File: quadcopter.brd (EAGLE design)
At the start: 128 x 128 mm, 67 parts, among them J1 ISP, J4 SIP-10_TH-254X10, M1 MOTOR_PADS, M2 MOTOR_PADS, M3 MOTOR_PADS, M4 MOTOR_PADS, SW1 PUSHBUTTON_SMD-VERTICAL-1, U1 ATMEGA128RFA1, Y1 16MHz

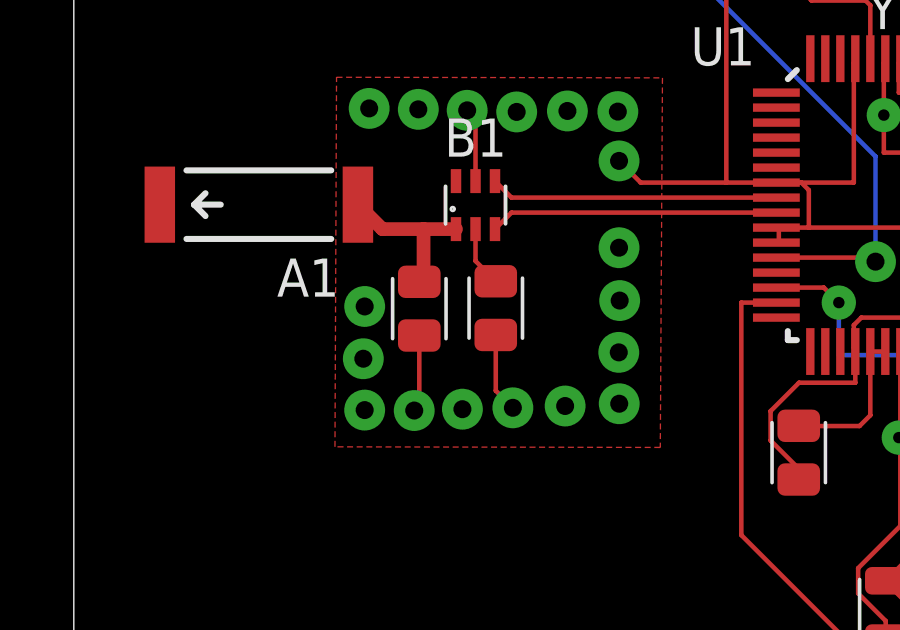
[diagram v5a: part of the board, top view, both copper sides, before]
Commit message: new board after Prof.'s review on May 10th
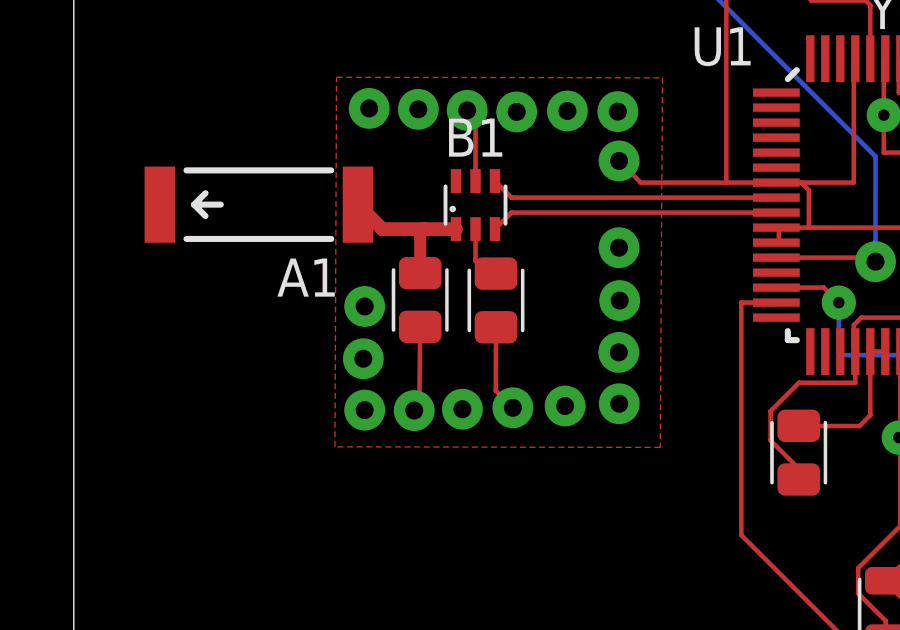
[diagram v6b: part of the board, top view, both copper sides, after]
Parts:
- moved C17 0.29 mm to (-38.5, -3.16)
- moved C15 0.26 mm to (-35.9, -3.18)
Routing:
- net GND: track 456.6 -> 457.2 mm
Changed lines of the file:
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@@
 <attribute name="MPN" value="GRM21A5C2E120JW01D" x="-20.88" y="12.74" size="1.778" layer="27" display="off"/>
 </element>
-<element name="C15" library="quadparts_prebuilt" package="CAPC2012X140_HS" value="22pF" x="-35.935" y="-3.434" rot="R270">
-<attribute name="CREATOR" value="PROF" x="-35.935" y="-3.434" size="1.778" layer="27" rot="R270" display="off"/>
-<attribute name="DIST" value="Digikey" x="-35.935" y="-3.434" size="1.778" layer="27" rot="R270" display="off"/>
-<attribute name="DISTPN" value="490-5534-1-ND" x="-35.935" y="-3.434" size="1.778" layer="27" rot="R270" display="off"/>
-<attribute name="MFR" value="Murata Electronics North America" x="-35.935" y="-3.434" size="1.778" layer="27" rot="R270" display="off"/>
-<attribute name="MPN" value="GRM21A5C2E220JW01D" x="-35.935" y="-3.434" size="1.778" layer="27" rot="R270" display="off"/>
-<attribute name="REVIEWER" value="" x="-35.935" y="-3.434" size="1.778" layer="27" rot="R270" display="off"/>
+<element name="C15" library="quadparts_prebuilt" package="CAPC2012X140_HS" value="22pF" x="-35.928" y="-3.178" rot="R270">
+<attribute name="CREATOR" value="PROF" x="-35.928" y="-3.178" size="1.778" layer="27" rot="R270" display="off"/>
+<attribute name="DIST" value="Digikey" x="-35.928" y="-3.178" size="1.778" layer="27" rot="R270" display="off"/>
+<attribute name="DISTPN" value="490-5534-1-ND" x="-35.928" y="-3.178" size="1.778" layer="27" rot="R270" display="off"/>
+<attribute name="MFR" value="Murata Electronics North America" x="-35.928" y="-3.178" size="1.778" layer="27" rot="R270" display="off"/>
+<attribute name="MPN" value="GRM21A5C2E220JW01D" x="-35.928" y="-3.178" size="1.778" layer="27" rot="R270" display="off"/>
+<attribute name="REVIEWER" value="" x="-35.928" y="-3.178" size="1.778" layer="27" rot="R270" display="off"/>
 </element>
 <element name="C16" library="quadparts_prebuilt" package="CAPC2012X140_HS" value="0.1uF" x="6.74" y="37.61" rot="R270">
@@
 <attribute name="REVIEWER" value="" x="6.74" y="37.61" size="1.778" layer="27" rot="R270" display="off"/>
 </element>
-<element name="C17" library="quadparts_prebuilt" package="CAPC2012X140_HS" value="0.75pF" x="-38.484" y="-3.452" rot="R90">
-<attribute name="DIST" value="Digikey" x="-38.484" y="-3.452" size="1.778" layer="27" rot="R90" display="off"/>
-<attribute name="DISTPN" value="490-3585-1-ND" x="-38.484" y="-3.452" size="1.778" layer="27" rot="R90" display="off"/>
-<attribute name="MFR" value="Murata Electronics North America" x="-38.484" y="-3.452" size="1.778" layer="27" rot="R90" display="off"/>
-<attribute name="MPN" value="GQM2195C2AR75CB01D" x="-38.484" y="-3.452" size="1.778" layer="27" rot="R90" display="off"/>
+<element name="C17" library="quadparts_prebuilt" package="CAPC2012X140_HS" value="0.75pF" x="-38.453" y="-3.163" rot="R90">
+<attribute name="DIST" value="Digikey" x="-38.453" y="-3.163" size="1.778" layer="27" rot="R90" display="off"/>
+<attribute name="DISTPN" value="490-3585-1-ND" x="-38.453" y="-3.163" size="1.778" layer="27" rot="R90" display="off"/>
+<attribute name="MFR" value="Murata Electronics North America" x="-38.453" y="-3.163" size="1.778" layer="27" rot="R90" display="off"/>
+<attribute name="MPN" value="GQM2195C2AR75CB01D" x="-38.453" y="-3.163" size="1.778" layer="27" rot="R90" display="off"/>
 </element>
 <element name="C18" library="quadparts_prebuilt" package="CAPC2012X140_HS" value="1uF" x="11.82" y="-16.16" rot="R90">
@@
 <via x="-40.35" y="-5.121" extent="1-16" drill="0.6"/>
 <via x="-40.305" y="-3.379" extent="1-16" drill="0.6"/>
-<wire x1="-38.484" y1="-4.347" x2="-38.484" y2="-6.679" width="0.1524" layer="1"/>
+<wire x1="-38.453" y1="-4.058" x2="-38.484" y2="-6.679" width="0.1524" layer="1"/>
 <wire x1="-38.484" y1="-6.679" x2="-38.653" y2="-6.848" width="0.1524" layer="1"/>
-<wire x1="-35.935" y1="-4.329" x2="-35.935" y2="-6.187" width="0.1524" layer="1"/>
+<wire x1="-35.928" y1="-4.073" x2="-35.935" y2="-6.187" width="0.1524" layer="1"/>
 <wire x1="-35.935" y1="-6.187" x2="-35.365" y2="-6.757" width="0.1524" layer="1"/>
 <wire x1="-36.61" y1="0.8" x2="-36.61" y2="2.881" width="0.1524" layer="1"/>
@@
 <contactref element="C17" pad="2"/>
 <contactref element="A1" pad="FEED"/>
-<wire x1="-37.26" y1="-0.8" x2="-38.343" y2="-0.8" width="0.4572" layer="1"/>
-<wire x1="-38.343" y1="-0.8" x2="-39.715" y2="-0.8" width="0.4572" layer="1"/>
+<wire x1="-37.26" y1="-0.8" x2="-38.319" y2="-0.8" width="0.4572" layer="1"/>
+<wire x1="-38.319" y1="-0.8" x2="-39.715" y2="-0.8" width="0.4572" layer="1"/>
 <wire x1="-39.715" y1="-0.8" x2="-40.53" y2="0.015" width="0.4572" layer="1"/>
-<wire x1="-38.343" y1="-0.8" x2="-38.343" y2="-2.416" width="0.4572" layer="1"/>
-<wire x1="-38.343" y1="-2.416" x2="-38.484" y2="-2.557" width="0.4572" layer="1"/>
+<wire x1="-38.453" y1="-2.268" x2="-38.343" y2="-2.416" width="0.4572" layer="1"/>
+<wire x1="-38.319" y1="-0.8" x2="-38.453" y2="-0.8" width="0.4064" layer="1"/>
+<wire x1="-38.453" y1="-0.8" x2="-38.453" y2="-2.268" width="0.4064" layer="1"/>
 </signal>
 <signal name="RESET">
@@
 <contactref element="C15" pad="1"/>
 <wire x1="-36.61" y1="-0.8" x2="-36.61" y2="-1.864" width="0.1524" layer="1"/>
-<wire x1="-36.61" y1="-1.864" x2="-35.935" y2="-2.539" width="0.1524" layer="1"/>
+<wire x1="-36.61" y1="-1.864" x2="-35.928" y2="-2.283" width="0.1524" layer="1"/>
 </signal>
 <signal name="N$16">

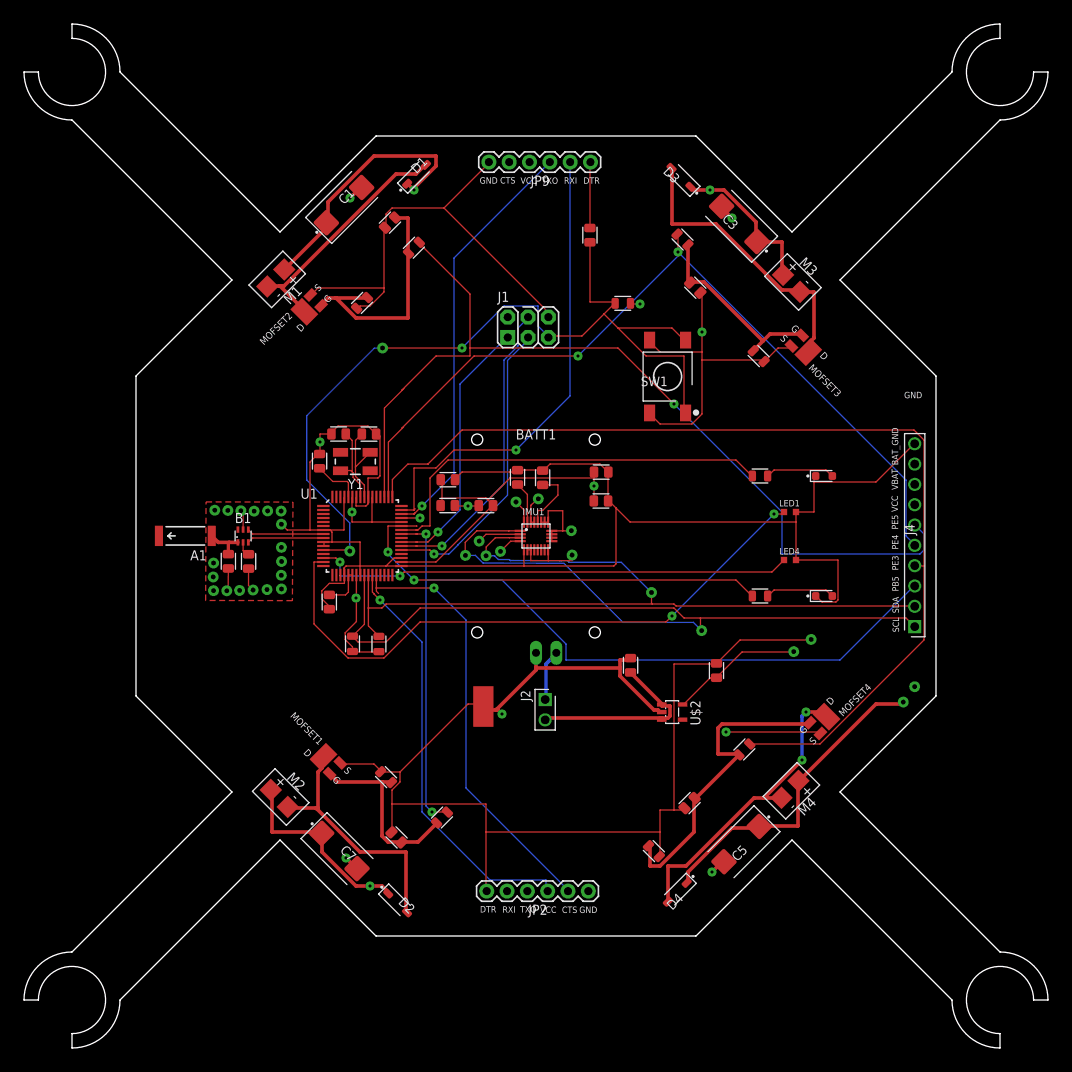
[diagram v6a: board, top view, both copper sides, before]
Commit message: New board with de cap connecting to microcon
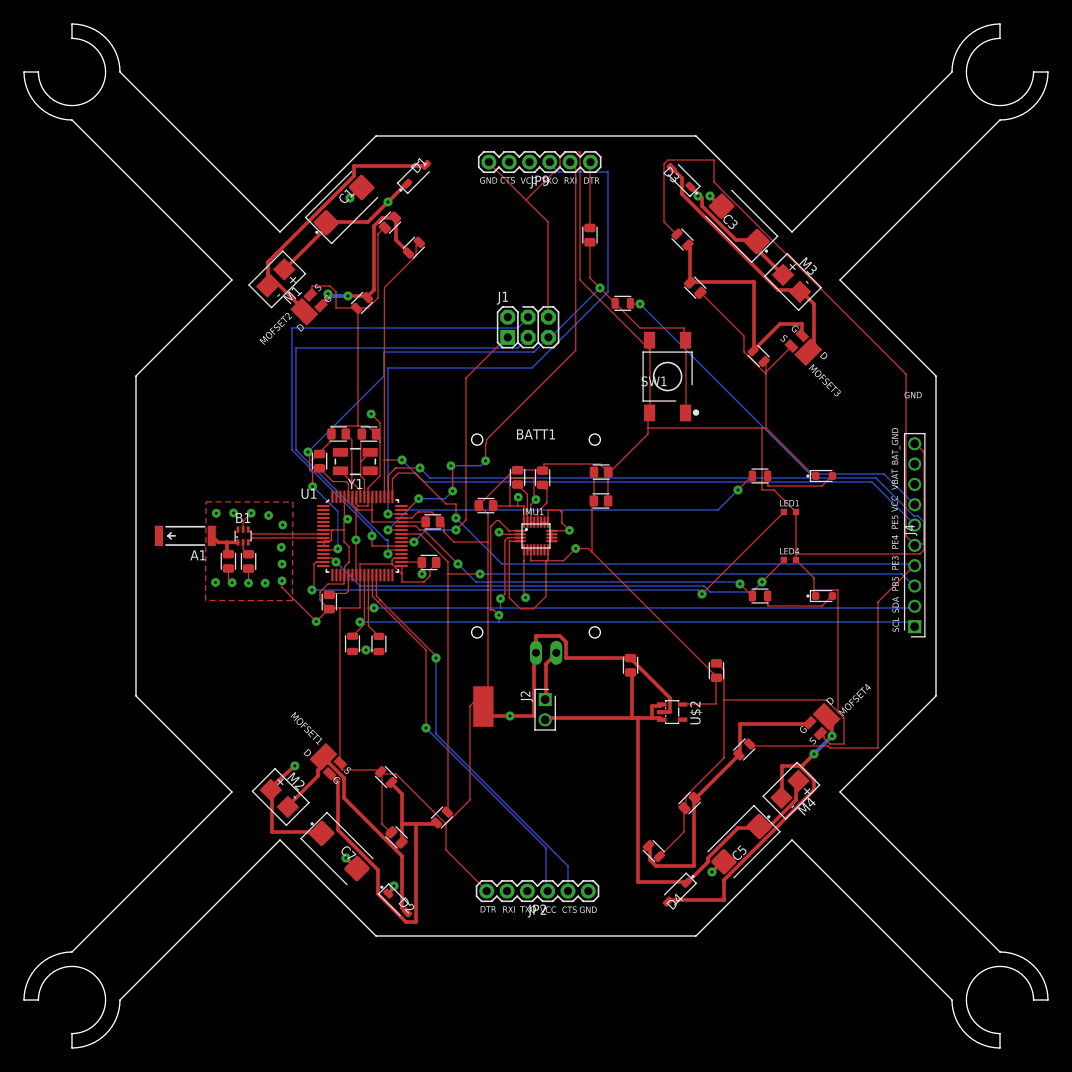
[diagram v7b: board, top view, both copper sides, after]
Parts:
- moved C11 10.6 mm to (-13.4, -3.31)
- moved C12 2.77 mm to (-12.9, 1.76)
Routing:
- net GND: track 457.2 -> 534.0 mm, vias 25 -> 17
- net VCC: track 119.2 -> 168.1 mm, vias 10 -> 8
- net PE4: track 104.5 -> 151.4 mm, vias 2 -> 1
- net SCL: track 125.7 -> 95.5 mm
- net MOSI: track 38.1 -> 65.2 mm
- net FILTERED_1: track 23.1 -> 48.4 mm
- net SCK: track 37.3 -> 62.4 mm
- net RX0: track 52.8 -> 74.3 mm
- net SDA: track 106.8 -> 87.4 mm
- net RESET: track 110.8 -> 91.9 mm, vias 3 -> 4
- net VBAT: track 142.2 -> 125.7 mm
- net PB5: track 110.3 -> 97.6 mm, vias 2 -> 1
- net PE5: track 116.0 -> 103.4 mm
- net PE3: track 125.1 -> 115.0 mm, vias 0 -> 1
- net PG1: track 77.0 -> 68.1 mm
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
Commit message: new board modified decoupling cap for imu
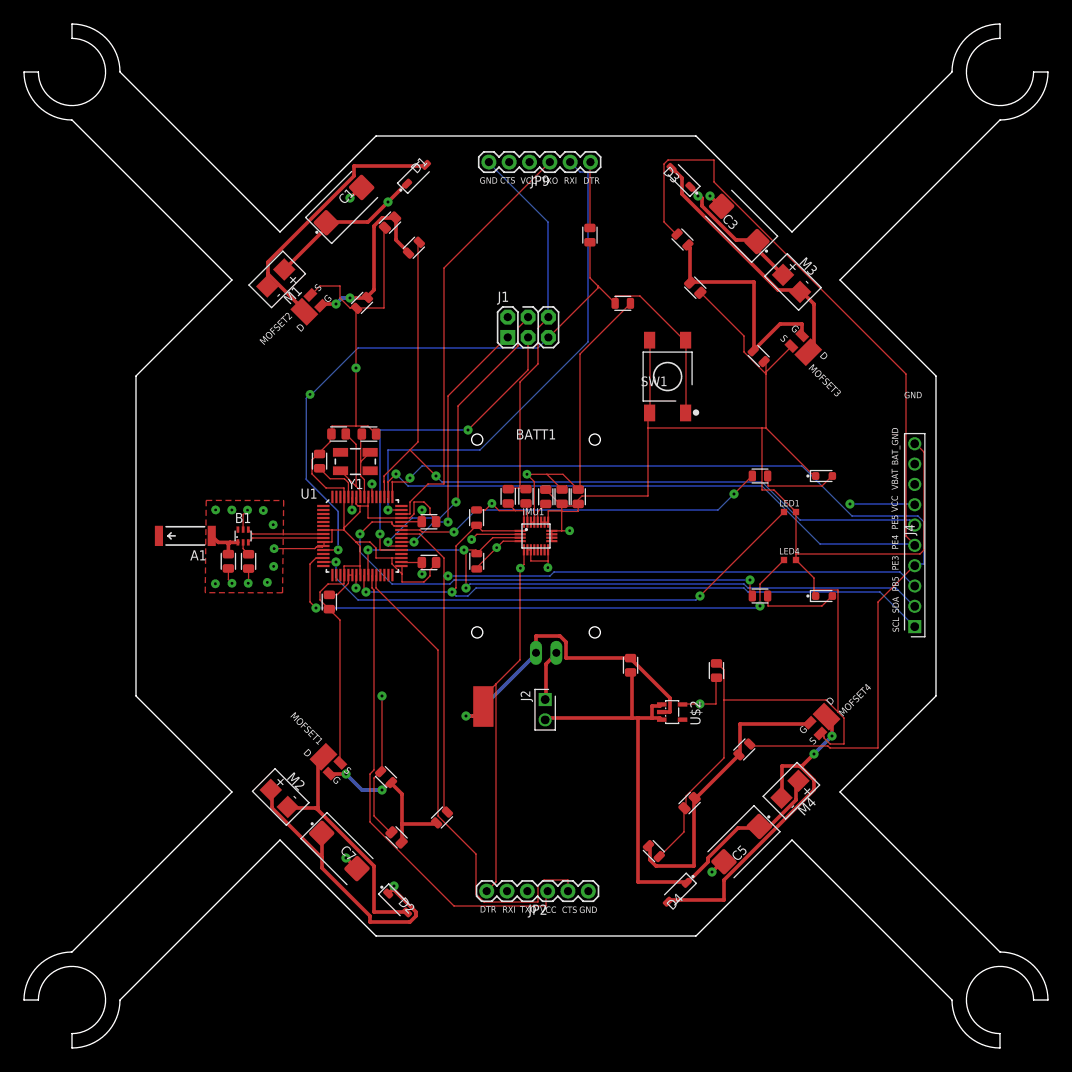
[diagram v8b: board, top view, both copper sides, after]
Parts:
- moved R14 22.1 mm to (-7.42, 2.30), turned to 90 degrees
- moved R15 16.0 mm to (-7.41, -3.16)
- moved C23 4.88 mm to (3.27, 4.92), turned to 90 degrees
- moved C22 4.21 mm to (5.28, 4.91), turned to 90 degrees
- moved C24 3.02 mm to (-3.48, 4.96), turned to 90 degrees
- moved C21 2.59 mm to (-1.26, 4.96)
- moved C20 2.41 mm to (1.22, 4.90)
- moved C12 0.49 mm to (-13.4, 1.78)
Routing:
- net VCC: track 168.1 -> 100.1 mm, vias 8 -> 12
- net GND: track 534.0 -> 488.0 mm, vias 17 -> 15
- net FILTERED_1: track 48.4 -> 21.5 mm, vias 0 -> 2
- net MOSI: track 65.2 -> 39.6 mm, vias 1 -> 2
- net RX0: track 74.3 -> 53.5 mm, vias 1 -> 0
- net VBAT: track 125.7 -> 145.4 mm, vias 4 -> 3
- net SCK: track 62.4 -> 43.4 mm, vias 1 -> 2
- net PB7: track 47.5 -> 61.2 mm
- net N$4: track 49.7 -> 60.7 mm, vias 1 -> 0
- net N$5: track 48.6 -> 59.5 mm, vias 1 -> 0
- net PG0: track 61.0 -> 70.4 mm
- net SCL: track 95.5 -> 88.8 mm
- net TX0: track 57.5 -> 63.8 mm, vias 4 -> 1
- net PE3: track 115.0 -> 120.1 mm
- net PE4: track 151.4 -> 146.5 mm
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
